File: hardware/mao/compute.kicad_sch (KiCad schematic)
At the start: 42 parts, among them J201 SERVICE, U201 ESP32-S3-WROOM-1-N8R2, U202 TCA6408ARGTR

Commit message: hardware: MAO_MAIN A0 routed board, fab package and final review
6-layer JLC06161H-3313 board (F / GND / signals / +3V3 / GND / B), routed from the
design scripts: designed power and fan-out copper, grid router with closed-set A*,
stub pruning, GND stitching (two ties on large pour fragments), tidy.
DRC 0 violations / 0 unconnected / 0 parity; ERC 0; silkscreen checker 0 findings.

- silkscreen: ODD JOBS mark and identity on both faces, S/N box, function-named
  test pads in a 3.0 x 3.2 mm service field; references for every semiconductor and
  connector plus the passives the service docs name, the rest on assembly drawings
- stackup, black mask, white legend and ENIG written into the board
- fab: 6-layer Gerbers + drill, JLC BOM (47 lines, LCSC on every line) and CPL
  (113 parts), assembly PDFs, FAB-NOTES with computed via counts
- docs: PCB, ODD JOBS and order-readiness review sections, final report, renders,
  factory-test pad map, bring-up and architecture updates

Co-Authored-By: Claude Opus 5.5 <noreply@anthropic.com>
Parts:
- added C205: 100nF 16V, Capacitor_SMD:C_0402_1005Metric, symbol Device:C
- added TP13: LCD, TestPoint:TestPoint_Pad_D1.0mm, symbol Connector:TestPoint
- added TP14: MIC, TestPoint:TestPoint_Pad_D1.0mm, symbol Connector:TestPoint
- added TP15: IRV, TestPoint:TestPoint_Pad_D1.0mm, symbol Connector:TestPoint
- added TP16: GND, MAO:TestPoint_Pad_D1.2mm, symbol Connector:TestPoint
- R203, R204: value 100k -> 1M; LCSC C25741 -> C26083; MPN 0402WGF1003TCE -> 0402WGF1004TCE
- R212: value 10k -> 100k; LCSC C25744 -> C25741; MPN 0402WGF1002TCE -> 0402WGF1003TCE
- TP1, TP2, TP3, TP4, TP5, TP6: footprint TestPoint:TestPoint_Pad_D1.5mm -> MAO:TestPoint_Pad_D1.2mm
- TP10, TP7, TP8, TP9: footprint TestPoint:TestPoint_Pad_D1.5mm -> TestPoint:TestPoint_Pad_D1.0mm
- TP11: value IO37 -> XRST
- TP12: value IO38 -> IO35
- U202: footprint Package_DFN_QFN:VQFN-16-1EP_3x3mm_P0.5mm_EP1.45x1.45mm -> Package_DFN_QFN:VQFN-16-1EP_3x3mm_P0.5mm_EP1.45x1.45mm_ThermalVias
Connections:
- net IO37_SPARE is gone; now on net EXP_RST_N: TP11.1, U201.30 (IO37)
- net +3V3: now also J201.4, C205.1; no longer C204.1, J201.1
- net AMP_BCLK: now also U201.10 (IO17); no longer U201.23 (IO21)
- net AMP_DIN: now also U201.9 (IO16); no longer U201.25 (IO48)
- net AMP_LRCLK: now also U201.11 (IO18); no longer U201.24 (IO47)
- net BOARD_ID: now also C204.1
- net EXP_INT_N: now also U201.23 (IO21); no longer U201.10 (IO17)
- net GND: now also J201.1, C205.2, TP16.1; no longer J201.5
- net HALL_A: now also U201.34 (IO41); no longer U201.32 (IO39)
- net HALL_B: now also U201.35 (IO42); no longer U201.33 (IO40)
- net I2C_SCL: now also U201.8 (IO15); no longer U201.9 (IO16)
- net I2C_SDA: now also U201.7 (IO7); no longer U201.8 (IO15)
- net IMU_INT2: now also U201.24 (IO47); no longer U201.7 (IO7)
- net IR_RX: now also U201.33 (IO40); no longer U201.29 (IO36)
- net IR_TX: now also U201.32 (IO39); no longer U201.28 (IO35)
- net MIC_CLK: now also U201.29 (IO36); no longer U201.34 (IO41)
- net MIC_DATA: now also U201.31 (IO38); no longer U201.35 (IO42)
- net PRESS_N: now also J201.6; no longer J201.3
- net TOF_INT_N: now also U201.25 (IO48); no longer U201.11 (IO18)
- net UART_RX: now also J201.5; no longer J201.6
- net UART_TX: now also J201.3; no longer J201.4
- net IO38_SPARE renamed IO35_SPARE
- net IO35_SPARE: now also U201.28 (IO35); no longer U201.31 (IO38)
- new net 3V3_LCD: TP13.1
- new net IR_RX_VCC: TP15.1
- new net MIC_VDD: TP14.1
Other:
- note added: "TXD0/RXD0 run straight from the module pins. Probe pads: rails beside the charger, comms in one field, switched rails at their sources (36-39)."
- note added: "Tag-Connect TC2030-NL (no part fitted): 1 GND, 2 EN, 3 TXD0, 4 3V3, 5 RXD0, 6 GPIO0 - recovery without USB (ODD JOBS 33-35, 157). Pinout chosen so"
- note removed: "Tag-Connect TC2030-NL (no part fitted): 1 3V3, 2 EN, 3 GPIO0, 4 TXD0, 5 GND, 6 RXD0 - recovery without USB (ODD JOBS 33-35, 157). Probe pads in one"
- note removed: "service field (36-38)."
- moved on the sheet: C204, FID1, FID2, FID3, FID4, FID5, FID6, H1, H2, H3

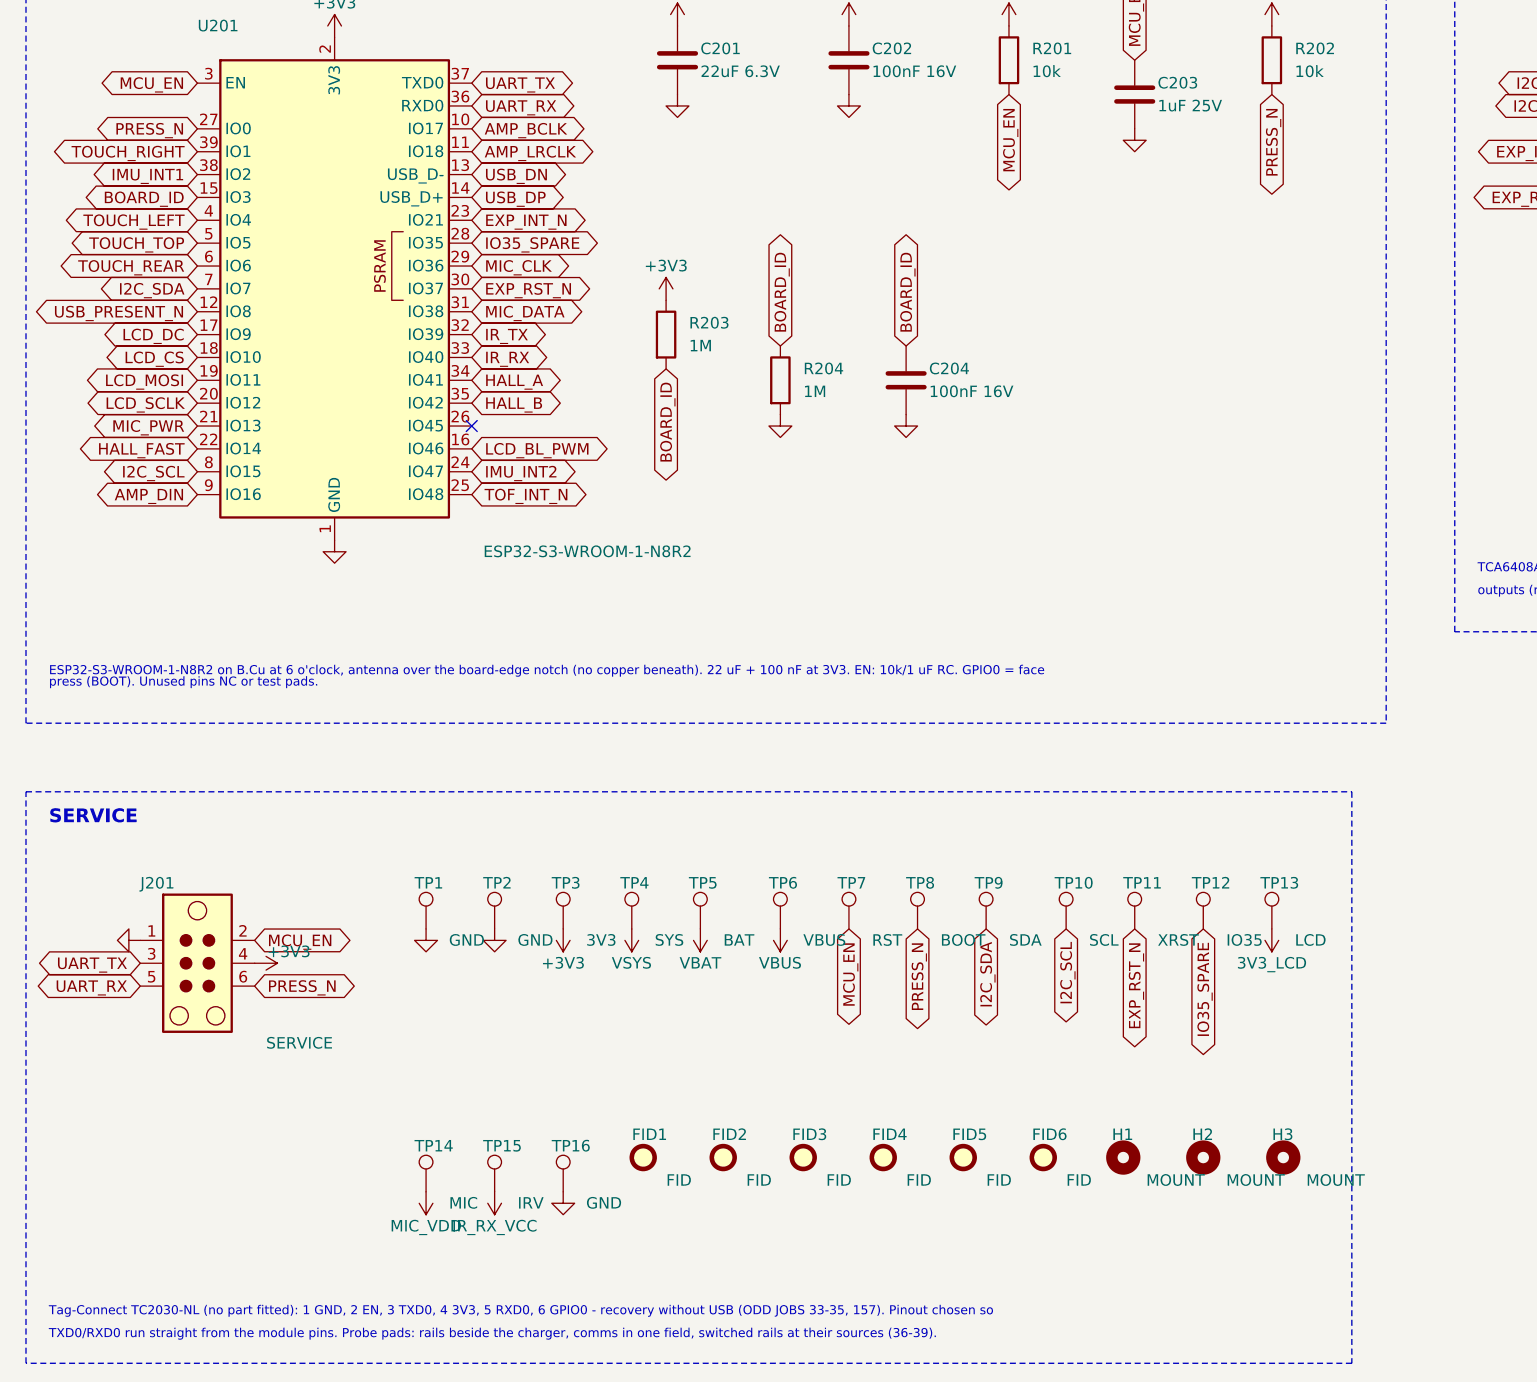
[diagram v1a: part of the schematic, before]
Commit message: hardware: MAO_MAIN A0 4-layer release, plug-in display, ODD JOBS review
- 4 layers (JLC04161H-1080): L1 parts + critical lines, L2 solid GND,
  L3 power regions + slow lines, L4 parts + lines. Re-placed and
  re-routed from scratch: 191 vias (6-layer board: 230).
- J301 HDGC 0.5K-HX-18PWB (C2919497): the round panel plugs in, no
  solder (Winstar 18-pin standard); display TE line added.
- 4-layer pin map; firmware header, pin-map doc and schematic notes
  generated from pinmap.py.
- Pipeline steps: power_regions, plane_check, via_off_pad, snap45 (all
  segments 0/45/90), models3d (datasheet-height bodies for every part).
- Checks: DRC/ERC/parity 0, every L2/L3 plane one piece, silk checker 0,
  Gerbers reviewed independently, firmware 5 configs 0 warnings.
- Mechanical: display standoff 2.7 mm for IR-receiver clearance, ToF
  light-blocking gasket, mic gasket tube, TOP-spring boss; panel tabs at
  2 and 8 o'clock.
- Docs: 4-layer design review, 200-rule ODD JOBS compliance, final
  report, layer plots, Gerber sheet, renders.

Co-Authored-By: Claude Opus 5.5 <noreply@anthropic.com>
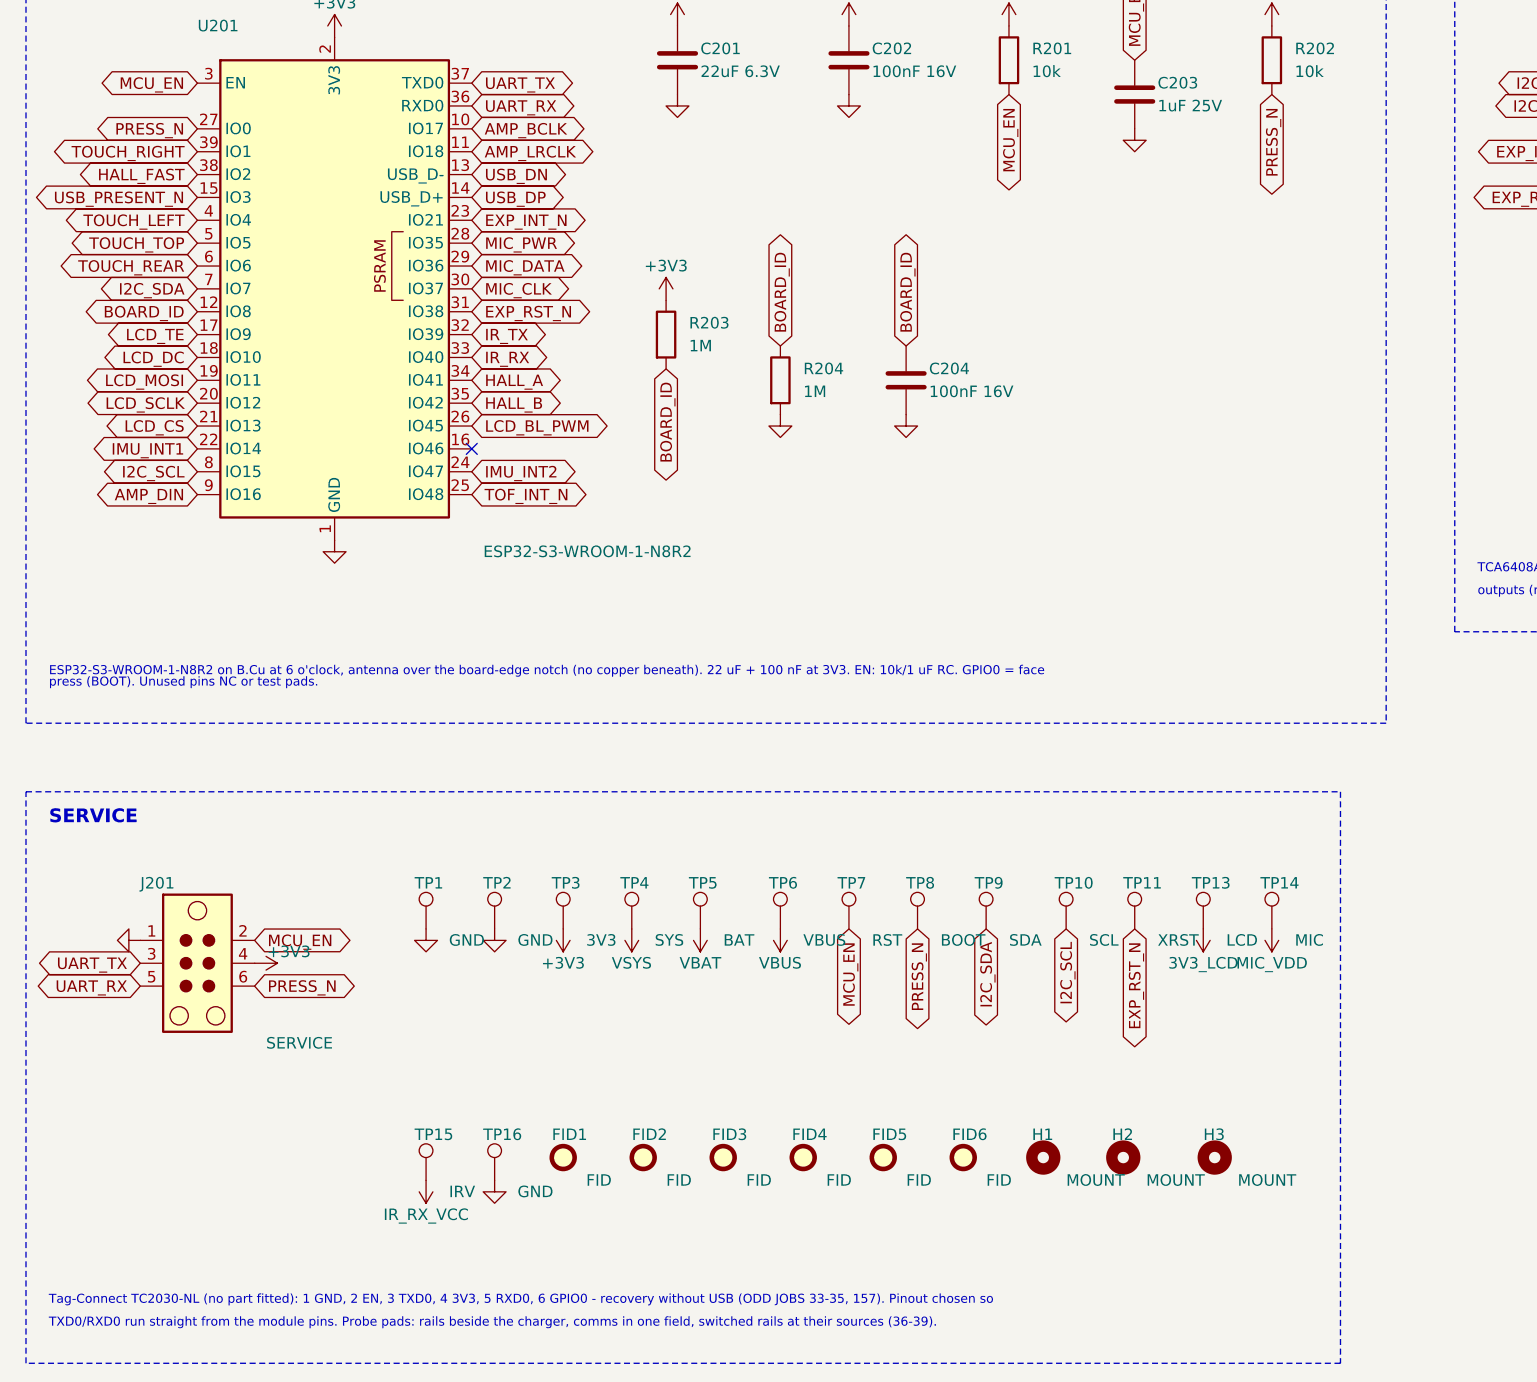
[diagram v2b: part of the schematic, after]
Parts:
- removed TP12: IO35, TestPoint:TestPoint_Pad_D1.0mm, symbol Connector:TestPoint
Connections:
- net IO35_SPARE is gone; now on net MIC_PWR: U201.28 (IO35)
- net BOARD_ID: now also U201.12 (IO8); no longer U201.15 (IO3)
- net EXP_RST_N: now also U201.31 (IO38); no longer U201.30 (IO37)
- net HALL_FAST: now also U201.38 (IO2); no longer U201.22 (IO14)
- net IMU_INT1: now also U201.22 (IO14); no longer U201.38 (IO2)
- net LCD_BL_PWM: now also U201.26 (IO45); no longer U201.16 (IO46)
- net LCD_CS: now also U201.21 (IO13); no longer U201.18 (IO10)
- net LCD_DC: now also U201.18 (IO10); no longer U201.17 (IO9)
- net MIC_CLK: now also U201.30 (IO37); no longer U201.29 (IO36)
- net MIC_DATA: now also U201.29 (IO36); no longer U201.31 (IO38)
- net MIC_PWR: no longer U201.21 (IO13)
- net USB_PRESENT_N: now also U201.15 (IO3); no longer U201.12 (IO8)
- new net LCD_TE: U201.17 (IO9)
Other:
- moved on the sheet: FID1, FID2, FID3, FID4, FID5, FID6, H1, H2, H3, TP13, TP14, TP15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

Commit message: MAO A0 revision: stock Winstar panel through a tail slot, AW9364 backlight, routed 4-layer board
Hardware changes from the verification audits:
- display: stock Winstar WF0128BTYAA4DNN0 (70 mm tail) through a routed slot at 9 o'clock
  to J301 on B.Cu; panel pin k on pad 19-k
- backlight: VLED+ on VSYS into an AW9364 (U303) constant-current sink, 40 mA nominal;
  Q301/R303-R305 removed
- display rail: TPS22919 (SC70-6, 1.1 mm: fits under the panel) with its VIN cap; CT cap gone
- +3V3 at 3.18 V (FB 536k), UVLO filter cap, charger ISET 4.3k (207 mA), /CE from the
  expander with a pull-down, charger moved to F under the panel, SD_MODE series 2.2k
- IR_TX on GPIO38, EXP_RST_N on GPIO39 (MTCK reset pull-up lit the IR LEDs)
- IR receiver and ToF pulled inside the ring lip; M2 boss / screw-head keep-outs

Layout: re-placed and re-routed. DRC 0 violations, 0 unconnected; every plane one piece
(the grid router now undoes any L3 route or via that splits a plane); 192 through vias.
Silk: type scale, 6 x 6 S/N field with the JLC order-number placeholder, 4.6 mm back mark,
references kept off vias, and a few easter eggs (a sleeping cat under the face, boop,
meow, 9 lives, MADE FOR BAD IDEAS).

Checks: ERC 0, silk text 0 findings, enclosure check 0 findings (mech_check.py), all
simulations pass (S3 AW9364, S10 TPS22919, S13 207 mA). Docs: bring-up, factory test,
power budget, architecture, mechanical (tail path), pin map. Firmware: dev command
"mao power charge off|on", self-test pad floor for the 3.18 V rail; merge patch regenerated.

Co-Authored-By: Claude Opus 5.5 <noreply@anthropic.com>
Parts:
- J201: value SERVICE -> TAG
- TP13: value LCD -> LCDV
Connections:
- net AMP_SD_N: no longer R208.1
- net EXP_RST_N: now also U201.32 (IO39); no longer U201.31 (IO38)
- net IR_TX: now also U201.31 (IO38); no longer U201.32 (IO39)
- net CHG_N renamed CHG_CE_N
- net LCD_BL_PWM renamed LCD_BL_CTRL
- new net AMP_SD: R208.1
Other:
- note added: "(BOOT). Unused pins NC or test pads."
- note added: "ESP32-S3-WROOM-1-N8R2 on B.Cu at 6 o'clock, antenna over the board-edge notch (no copper beneath). 22 uF + 100 nF at 3V3. EN: 10k/1 uF RC. GPIO0 = face press"
- note removed: "ESP32-S3-WROOM-1-N8R2 on B.Cu at 6 o'clock, antenna over the board-edge notch (no copper beneath). 22 uF + 100 nF at 3V3. EN: 10k/1 uF RC. GPIO0 = face"
- note removed: "press (BOOT). Unused pins NC or test pads."
- moved on the sheet: C203, C204, C205, R201, R202, R203, R204, R205, R206, R207, R208, R209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
